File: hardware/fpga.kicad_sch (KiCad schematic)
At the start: 12 parts, among them Q3 AO3400A, Q4 AO3400A, U1 ICE40HX4K-TQ144

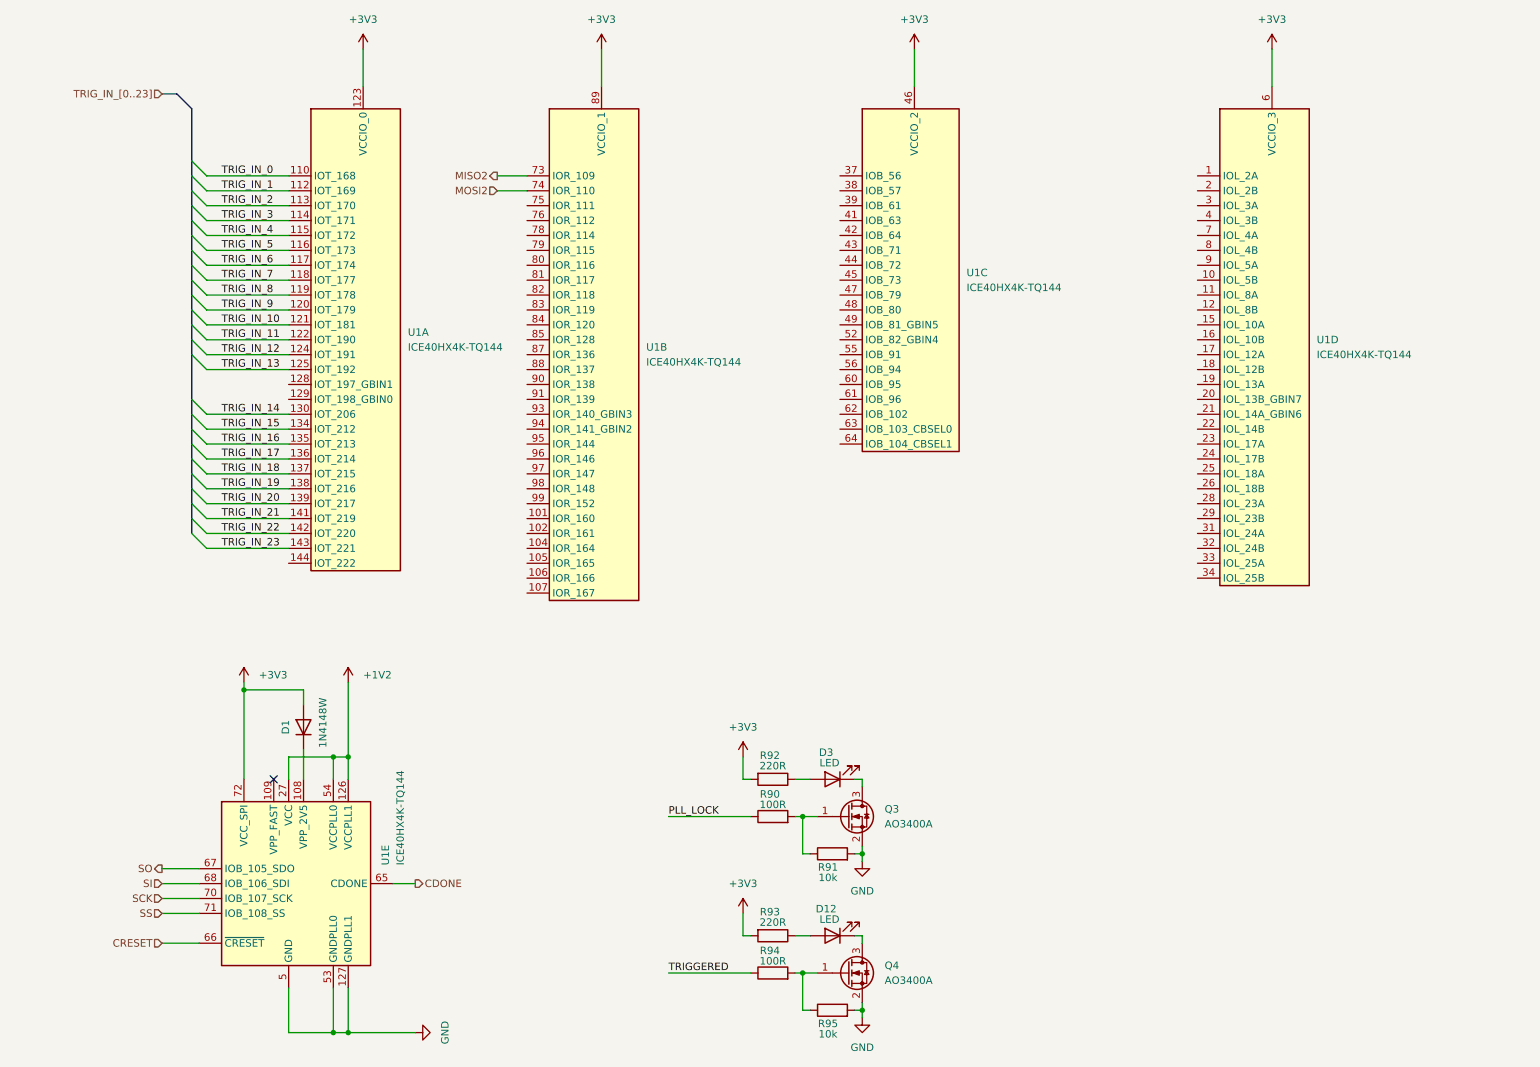
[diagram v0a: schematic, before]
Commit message: complete schematic wiring
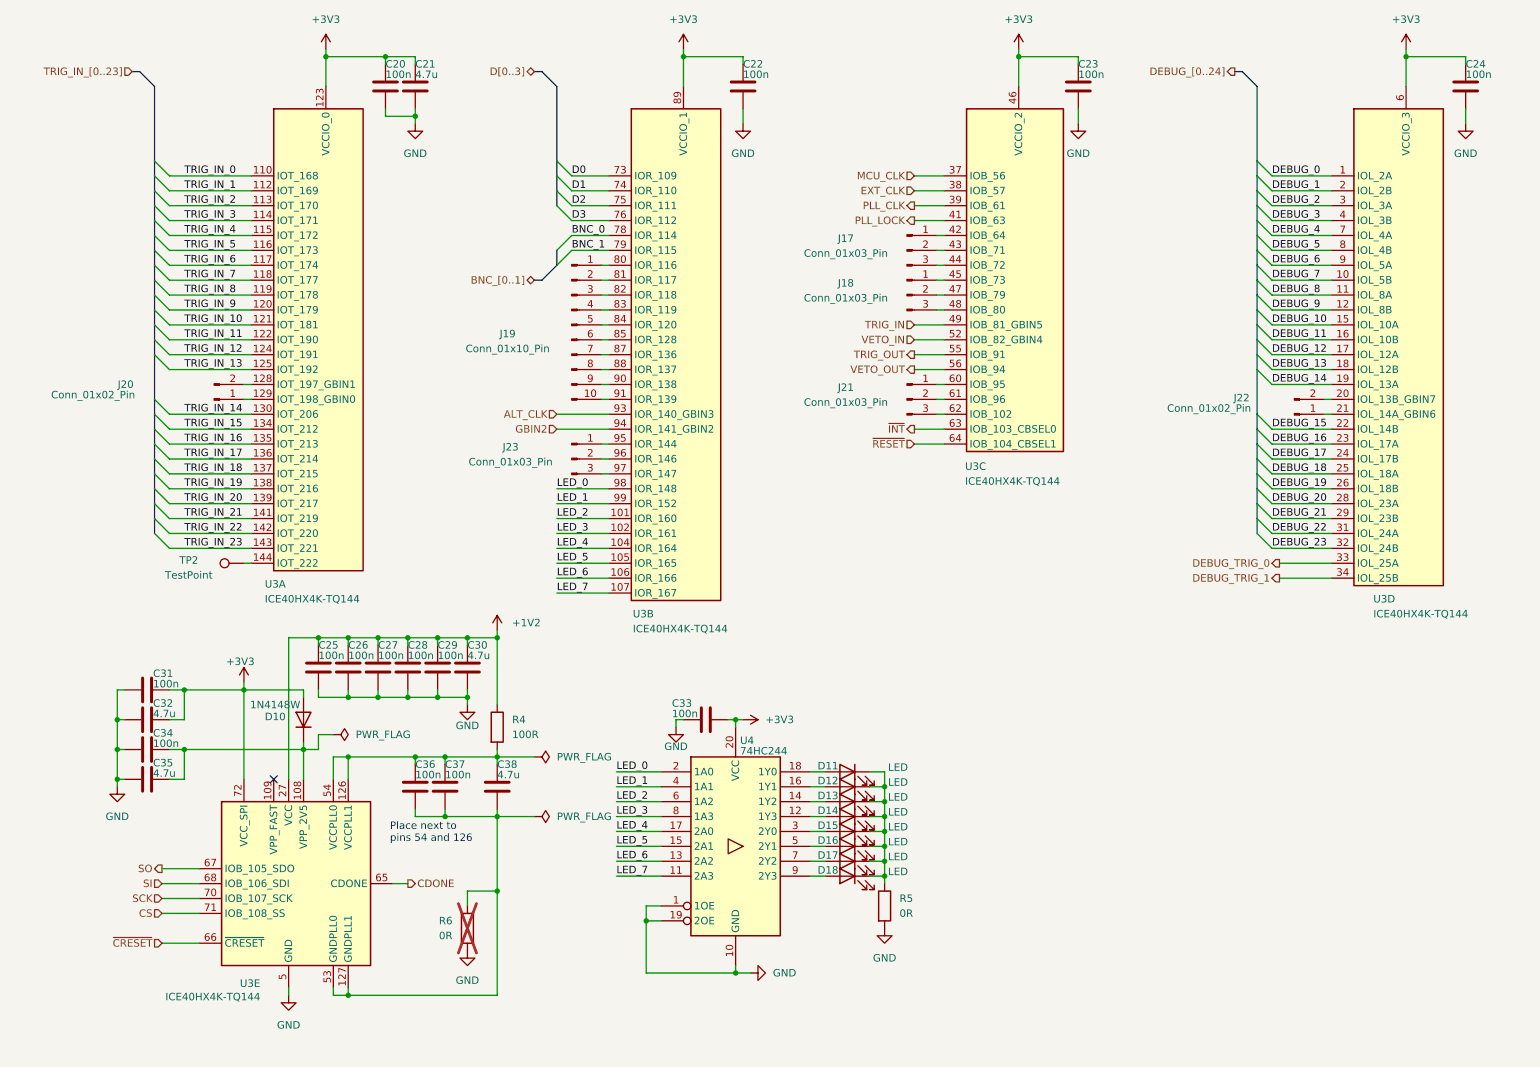
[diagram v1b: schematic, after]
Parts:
- removed D3: LED, symbol Device:LED
- removed Q3, Q4: AO3400A, symbol Transistor_FET:Q_NMOS_GSD
- removed R90, R94: 100R, symbol Device:R
- removed R91, R95: 10k, symbol Device:R
- removed R92, R93: 220R, symbol Device:R
- added C20, C22, C23, C24, C25, C26, C27, C28, C29, C31, C33, C34, C36, C37: 100n, symbol Device:C
- added C21, C30, C32, C35, C38: 4.7u, symbol Device:C
- added D11, D13, D14, D15, D16, D17, D18: LED, symbol Device:LED
- added J17, J18, J21, J23: Conn_01x03_Pin, symbol Connector:Conn_01x03_Pin
- added J19: Conn_01x10_Pin, symbol Connector:Conn_01x10_Pin
- added J20, J22: Conn_01x02_Pin, symbol Connector:Conn_01x02_Pin
- added R4: 100R, symbol Device:R
- added R5, R6: 0R, symbol Device:R
- added TP2: TestPoint, symbol Connector:TestPoint
- added U4: 74HC244, symbol 74xx:74HC244
- renumbered D1 to D10, U1 to U3
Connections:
- net +1V2: now also C25.1, C26.1, C27.1, C28.1, C29.1, C30.1, R4.1; no longer U3.126 (VCCPLL1), U3.54 (VCCPLL0)
- net +3V3: now also C20.1, C21.1, C22.1, C23.1, C24.1, C31.1, C32.1, C33.2, U4.20 (VCC)
- net GND: now also C20.2, C21.2, C22.2, C23.2, C24.2, C25.2, C26.2, C27.2, C28.2, C29.2, C30.2, C31.2, C32.2, C33.1, C34.2, C35.2, R5.2, R6.2, U4.1 (1OE), U4.10 (GND), U4.19 (2OE); no longer U3.127 (GNDPLL1), U3.53 (GNDPLL0)
- net PLL_LOCK: now also U3.41 (IOB_63)
- net MCU_CLK: now reaches U3.37 (IOB_56)
- net EXT_CLK: now reaches U3.38 (IOB_57)
- net PLL_CLK: now reaches U3.39 (IOB_61)
- net at U3.42 (IOB_64): now also J17.1 (Pin_1)
- net at U3.43 (IOB_71): now also J17.2 (Pin_2)
- net at U3.44 (IOB_72): now also J17.3 (Pin_3)
- net at U3.45 (IOB_73): now also J18.1 (Pin_1)
- net at U3.47 (IOB_79): now also J18.2 (Pin_2)
- net at U3.48 (IOB_80): now also J18.3 (Pin_3)
- net TRIG_IN: now reaches U3.49 (IOB_81_GBIN5)
- net VETO_IN: now reaches U3.52 (IOB_82_GBIN4)
- net TRIG_OUT: now reaches U3.55 (IOB_91)
- net VETO_OUT: now reaches U3.56 (IOB_94)
- net at U3.60 (IOB_95): now also J21.1 (Pin_1)
- net at U3.61 (IOB_96): now also J21.2 (Pin_2)
- net at U3.62 (IOB_102): now also J21.3 (Pin_3)
- net ~{INT}: now reaches U3.63 (IOB_103_CBSEL0)
- net ~{RESET}: now reaches U3.64 (IOB_104_CBSEL1)
- net at U3.128 (IOT_197_GBIN1): now also J20.2 (Pin_2)
- net at U3.129 (IOT_198_GBIN0): now also J20.1 (Pin_1)
- net at U3.144 (IOT_222): now also TP2.1
- net DEBUG_0: now reaches U3.1 (IOL_2A)
- net DEBUG_7: now reaches U3.10 (IOL_5B)
- net DEBUG_8: now reaches U3.11 (IOL_8A)
- net DEBUG_9: now reaches U3.12 (IOL_8B)
- net DEBUG_10: now reaches U3.15 (IOL_10A)
- net DEBUG_11: now reaches U3.16 (IOL_10B)
- net DEBUG_12: now reaches U3.17 (IOL_12A)
- net DEBUG_13: now reaches U3.18 (IOL_12B)
- net DEBUG_14: now reaches U3.19 (IOL_13A)
- net DEBUG_1: now reaches U3.2 (IOL_2B)
- net at U3.20 (IOL_13B_GBIN7): now also J22.2 (Pin_2)
- net at U3.21 (IOL_14A_GBIN6): now also J22.1 (Pin_1)
- net DEBUG_15: now reaches U3.22 (IOL_14B)
- net DEBUG_16: now reaches U3.23 (IOL_17A)
- net DEBUG_17: now reaches U3.24 (IOL_17B)
- net DEBUG_18: now reaches U3.25 (IOL_18A)
- net DEBUG_19: now reaches U3.26 (IOL_18B)
- net DEBUG_20: now reaches U3.28 (IOL_23A)
- net DEBUG_21: now reaches U3.29 (IOL_23B)
- net DEBUG_2: now reaches U3.3 (IOL_3A)
- net DEBUG_22: now reaches U3.31 (IOL_24A)
- net DEBUG_23: now reaches U3.32 (IOL_24B)
- net DEBUG_TRIG_0: now reaches U3.33 (IOL_25A)
- net DEBUG_TRIG_1: now reaches U3.34 (IOL_25B)
- net DEBUG_3: now reaches U3.4 (IOL_3B)
- net DEBUG_4: now reaches U3.7 (IOL_4A)
- net DEBUG_5: now reaches U3.8 (IOL_4B)
- net DEBUG_6: now reaches U3.9 (IOL_5A)
- net LED_2: now reaches U3.101 (IOR_160)
- net LED_2: now also U4.6 (1A2)
- net LED_3: now reaches U3.102 (IOR_161)
- net LED_3: now also U4.8 (1A3)
- net LED_4: now reaches U3.104 (IOR_164)
- net LED_4: now also U4.17 (2A0)
- net LED_5: now reaches U3.105 (IOR_165)
- net LED_5: now also U4.15 (2A1)
- net LED_6: now reaches U3.106 (IOR_166)
- net LED_6: now also U4.13 (2A2)
- net LED_7: now reaches U3.107 (IOR_167)
- net LED_7: now also U4.11 (2A3)
- net D2: now reaches U3.75 (IOR_111)
- net D3: now reaches U3.76 (IOR_112)
- net BNC_0: now reaches U3.78 (IOR_114)
- net BNC_1: now reaches U3.79 (IOR_115)
- net at U3.80 (IOR_116): now also J19.1 (Pin_1)
- net at U3.81 (IOR_117): now also J19.2 (Pin_2)
- net at U3.82 (IOR_118): now also J19.3 (Pin_3)
- net at U3.83 (IOR_119): now also J19.4 (Pin_4)
- net at U3.84 (IOR_120): now also J19.5 (Pin_5)
- net at U3.85 (IOR_128): now also J19.6 (Pin_6)
- net at U3.87 (IOR_136): now also J19.7 (Pin_7)
- net at U3.88 (IOR_137): now also J19.8 (Pin_8)
- net at U3.90 (IOR_138): now also J19.9 (Pin_9)
- net at U3.91 (IOR_139): now also J19.10 (Pin_10)
- net ALT_CLK: now reaches U3.93 (IOR_140_GBIN3)
- net GBIN2: now reaches U3.94 (IOR_141_GBIN2)
- net at U3.95 (IOR_144): now also J23.1 (Pin_1)
- net at U3.96 (IOR_146): now also J23.2 (Pin_2)
- net at U3.97 (IOR_147): now also J23.3 (Pin_3)
- net LED_0: now reaches U3.98 (IOR_148)
- net LED_0: now also U4.2 (1A0)
- net LED_1: now reaches U3.99 (IOR_152)
- net LED_1: now also U4.4 (1A1)
- net at D12.1 (K): now also D11.1 (K), D13.1 (K), D14.1 (K), D15.1 (K), D16.1 (K), D17.1 (K), D18.1 (K), R5.1
- net at D12.2 (A): now also U4.16 (1Y1)
- net at D10.1 (K), U3.108 (VPP_2V5): now also C34.1, C35.1
- net CRESET renamed ~{CRESET}
- net MISO2 renamed D0
- net MOSI2 renamed D1
- net SS renamed CS
- new net: C36.1, C37.1, C38.1, R4.2, U3.126 (VCCPLL1), U3.54 (VCCPLL0)
- new net: C36.2, C37.2, C38.2, R6.1, U3.127 (GNDPLL1), U3.53 (GNDPLL0)
- new net: D15.2 (A), U4.3 (2Y0)
- new net: D14.2 (A), U4.12 (1Y3)
- new net: D13.2 (A), U4.14 (1Y2)
- new net: D11.2 (A), U4.18 (1Y0)
- new net: D16.2 (A), U4.5 (2Y1)
- new net: D17.2 (A), U4.7 (2Y2)
- new net: D18.2 (A), U4.9 (2Y3)
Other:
- note added: "Place next to pins 54 and 126"
- moved on the sheet: D10, U3A, U3B, U3C, U3D

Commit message: update power system + add LCSC part numbers
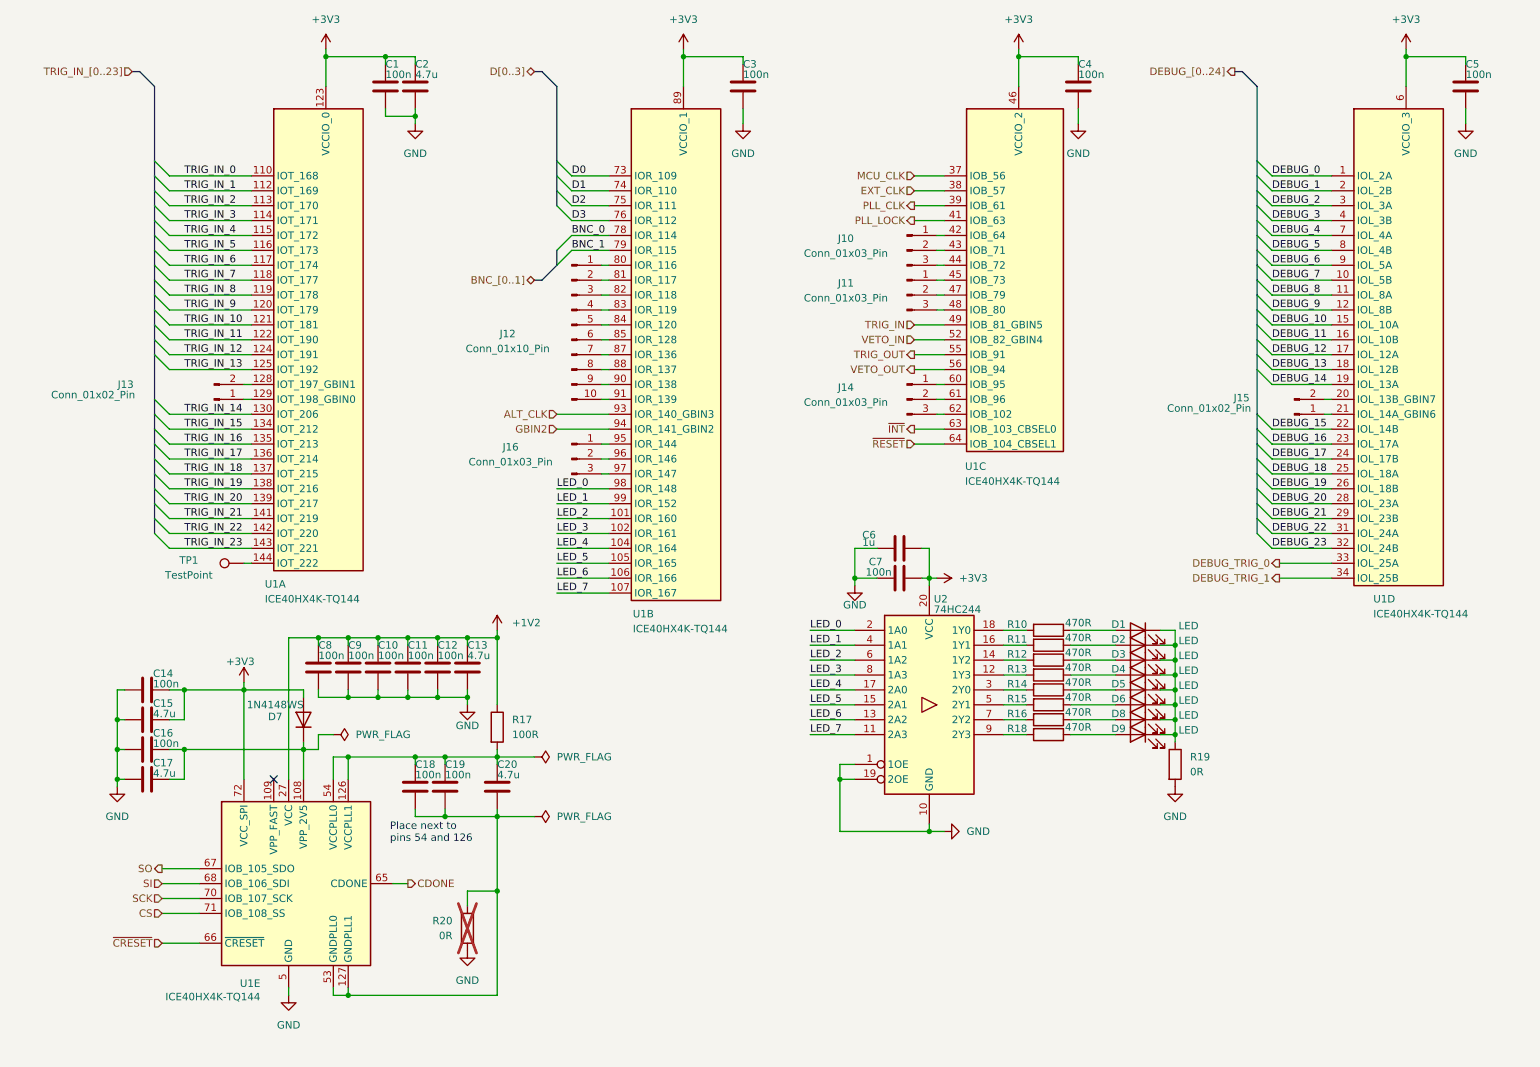
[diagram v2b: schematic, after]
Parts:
- added C6: 1u, Capacitor_SMD:C_0805_2012Metric, symbol Device:C
- added R10, R11, R12, R13, R14, R15, R16, R18: 470R, Resistor_SMD:R_0402_1005Metric, symbol Device:R
- C1: renamed from C20; footprint (none) -> Capacitor_SMD:C_0402_1005Metric; LCSC (none) -> C307331
- C10: renamed from C27; footprint (none) -> Capacitor_SMD:C_0402_1005Metric; LCSC (none) -> C307331
- C11: renamed from C28; footprint (none) -> Capacitor_SMD:C_0402_1005Metric; LCSC (none) -> C307331
- C12: renamed from C29; footprint (none) -> Capacitor_SMD:C_0402_1005Metric; LCSC (none) -> C307331
- C13: renamed from C30; footprint (none) -> Capacitor_SMD:C_1206_3216Metric; LCSC (none) -> C29823
- C14: renamed from C31; footprint (none) -> Capacitor_SMD:C_0402_1005Metric; LCSC (none) -> C307331
- C15: renamed from C32; footprint (none) -> Capacitor_SMD:C_1206_3216Metric; LCSC (none) -> C29823
- C16: renamed from C34; footprint (none) -> Capacitor_SMD:C_0402_1005Metric; LCSC (none) -> C307331
- C17: renamed from C35; footprint (none) -> Capacitor_SMD:C_1206_3216Metric; LCSC (none) -> C29823
- C18: renamed from C36; footprint (none) -> Capacitor_SMD:C_0402_1005Metric; LCSC (none) -> C307331
- C19: renamed from C37; footprint (none) -> Capacitor_SMD:C_0402_1005Metric; LCSC (none) -> C307331
- C2: renamed from C21; footprint (none) -> Capacitor_SMD:C_1206_3216Metric; LCSC (none) -> C29823
- C20: renamed from C38; footprint (none) -> Capacitor_SMD:C_1206_3216Metric; LCSC (none) -> C29823
- C3: renamed from C22; footprint (none) -> Capacitor_SMD:C_0402_1005Metric; LCSC (none) -> C307331
- C4: renamed from C23; footprint (none) -> Capacitor_SMD:C_0402_1005Metric; LCSC (none) -> C307331
- C5: renamed from C24; footprint (none) -> Capacitor_SMD:C_0402_1005Metric; LCSC (none) -> C307331
- C7: renamed from C33; footprint (none) -> Capacitor_SMD:C_0402_1005Metric; LCSC (none) -> C307331
- C8: renamed from C25; footprint (none) -> Capacitor_SMD:C_0402_1005Metric; LCSC (none) -> C307331
- C9: renamed from C26; footprint (none) -> Capacitor_SMD:C_0402_1005Metric; LCSC (none) -> C307331
- D1: renamed from D11; footprint (none) -> LED_SMD:LED_0805_2012Metric; LCSC (none) -> C2297
- D2: renamed from D12; footprint (none) -> LED_SMD:LED_0805_2012Metric; LCSC (none) -> C2297
- D3: renamed from D13; footprint (none) -> LED_SMD:LED_0805_2012Metric; LCSC (none) -> C2297
- D4: renamed from D14; footprint (none) -> LED_SMD:LED_0805_2012Metric; LCSC (none) -> C2297
- D5: renamed from D15; footprint (none) -> LED_SMD:LED_0805_2012Metric; LCSC (none) -> C2297
- D6: renamed from D16; footprint (none) -> LED_SMD:LED_0805_2012Metric; LCSC (none) -> C2297
- D7: renamed from D10; value 1N4148W -> 1N4148WS; footprint (none) -> Diode_SMD:D_SOD-323; LCSC (none) -> C2128
- D8: renamed from D17; footprint (none) -> LED_SMD:LED_0805_2012Metric; LCSC (none) -> C2297
- D9: renamed from D18; footprint (none) -> LED_SMD:LED_0805_2012Metric; LCSC (none) -> C2297
- J10: renamed from J17; footprint (none) -> Connector_PinHeader_2.54mm:PinHeader_1x03_P2.54mm_Vertical
- J11: renamed from J18; footprint (none) -> Connector_PinHeader_2.54mm:PinHeader_1x03_P2.54mm_Vertical
- J12: renamed from J19; footprint (none) -> Connector_PinHeader_2.54mm:PinHeader_1x10_P2.54mm_Vertical
- J13: renamed from J20; footprint (none) -> Connector_PinHeader_2.54mm:PinHeader_1x02_P2.54mm_Vertical
- J14: renamed from J21; footprint (none) -> Connector_PinHeader_2.54mm:PinHeader_1x03_P2.54mm_Vertical
- J15: renamed from J22; footprint (none) -> Connector_PinHeader_2.54mm:PinHeader_1x02_P2.54mm_Vertical
- J16: renamed from J23; footprint (none) -> Connector_PinHeader_2.54mm:PinHeader_1x03_P2.54mm_Vertical
- R17: renamed from R4; footprint (none) -> Resistor_SMD:R_0402_1005Metric; LCSC (none) -> C25076
- R19: renamed from R5; footprint (none) -> Resistor_SMD:R_0402_1005Metric; LCSC (none) -> C17168
- R20: renamed from R6; footprint (none) -> Resistor_SMD:R_0603_1608Metric; LCSC (none) -> C21189
- TP1: renamed from TP2; footprint (none) -> TestPoint:TestPoint_Pad_D1.0mm
- U2: renamed from U4; footprint (none) -> Package_SO:TSSOP-20_4.4x6.5mm_P0.65mm; LCSC (none) -> C6835
- renumbered U3 to U1
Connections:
- net +3V3: now also C6.2
- net GND: now also C6.1
- net at D2.2 (A): now also R11.1; no longer U2.16 (1Y1)
- net at D5.2 (A): now also R14.1; no longer U2.3 (2Y0)
- net at D4.2 (A): now also R13.1; no longer U2.12 (1Y3)
- net at U2.14 (1Y2): now also R12.2; no longer D3.2 (A)
- net at D1.2 (A): now also R10.1; no longer U2.18 (1Y0)
- net at D6.2 (A): now also R15.1; no longer U2.5 (2Y1)
- net at D8.2 (A): now also R16.1; no longer U2.7 (2Y2)
- net at D9.2 (A): now also R18.1; no longer U2.9 (2Y3)
- new net: R11.2, U2.16 (1Y1)
- new net: R15.2, U2.5 (2Y1)
- new net: R18.2, U2.9 (2Y3)
- new net: R10.2, U2.18 (1Y0)
- new net: R16.2, U2.7 (2Y2)
- new net: R13.2, U2.12 (1Y3)
- new net: R14.2, U2.3 (2Y0)
- new net: D3.2 (A), R12.1
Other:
- moved on the sheet: C7, D1, D2, D3, D4, D5, D6, D8, D9, R19, U2

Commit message: route more
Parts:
- removed J13: Conn_01x02_Pin, Connector_PinHeader_2.54mm:PinHeader_1x02_P2.54mm_Vertical, symbol Connector:Conn_01x02_Pin
- added C147, C148: 100n, Capacitor_SMD:C_0402_1005Metric, symbol Device:C
- added TP43, TP44: TestPoint, TestPoint:TestPoint_Pad_D1.0mm, symbol Connector:TestPoint
- J10, J11, J14, J16: footprint Connector_PinHeader_2.54mm:PinHeader_1x03_P2.54mm_Vertical -> Connector_PinHeader_1.00mm:PinHeader_1x03_P1.00mm_Vertical_SMD_Pin1Left
- J12: footprint Connector_PinHeader_2.54mm:PinHeader_1x10_P2.54mm_Vertical -> Connector_PinHeader_1.00mm:PinHeader_1x10_P1.00mm_Vertical_SMD_Pin1Left
- J15: footprint Connector_PinHeader_2.54mm:PinHeader_1x02_P2.54mm_Vertical -> Connector_PinHeader_1.00mm:PinHeader_1x02_P1.00mm_Vertical_SMD_Pin1Left
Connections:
- net +1V2: no longer C12.1, C9.1
- net +3V3: now also C12.1, C9.1, C147.1, C148.1
- net GND: now also C147.2, C148.2
- net at U1.128 (IOT_197_GBIN1): now also TP43.1
- net at U1.129 (IOT_198_GBIN0): now also TP44.1
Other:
- moved on the sheet: C10, C11, C8
